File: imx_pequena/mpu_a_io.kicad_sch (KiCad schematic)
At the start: 1 part, among them U1 MCIMX6Z0DVM09AB

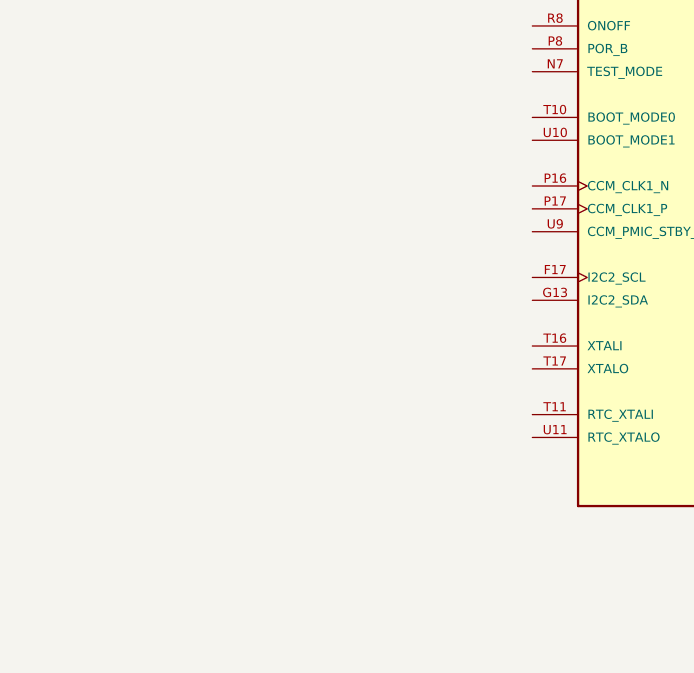
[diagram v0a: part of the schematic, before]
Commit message: Started IO section
began adding crystals
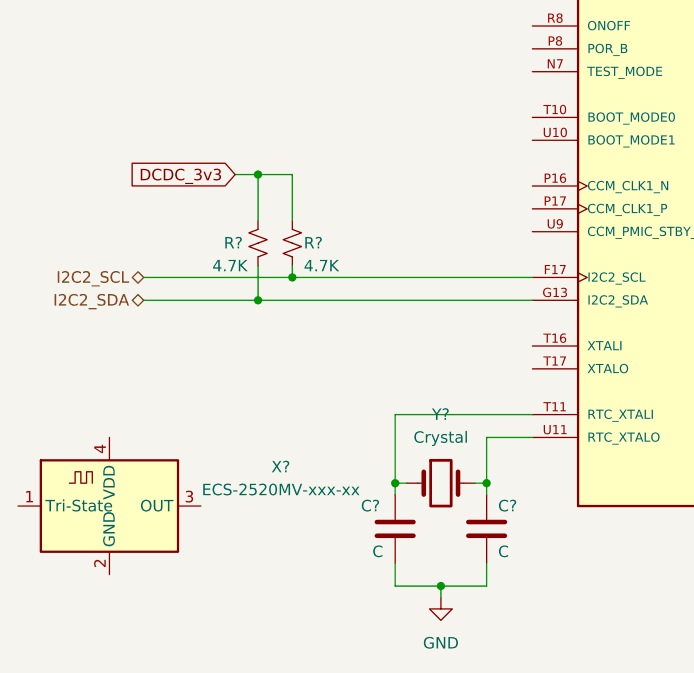
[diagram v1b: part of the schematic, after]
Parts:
- added C? (x2): C, symbol Device:C
- added R? (x2): 4.7K, symbol Device:R_Small_US
- added X?: ECS-2520MV-xxx-xx, Oscillator:Oscillator_SMD_ECS_2520MV-xxx-xx-4Pin_2.5x2.0mm, symbol Oscillator:ECS-2520MV-xxx-xx
- added Y?: Crystal, symbol Device:Crystal
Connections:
- net I2C2_SCL: now reaches U1.F17 (I2C2_SCL)
- net I2C2_SCL: now also R?.2
- net I2C2_SDA: now reaches U1.G13 (I2C2_SDA)
- net I2C2_SDA: now also R?.2
- net at U1.T11 (RTC_XTALI): now also C?.1, Y?.1
- net at U1.U11 (RTC_XTALO): now also C?.1, Y?.2
- new net DCDC_3v3: R?.1, R?.1
- new net GND: C?.2, C?.2
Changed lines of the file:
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@@
 (kicad_sch (version 20211123) (generator eeschema)
   (paper "A4")
+  (junction (at 93.98 114.3) (diameter 0) (color 0 0 0 0)
+  )
+  (junction (at 104.14 114.3) (diameter 0) (color 0 0 0 0)
+  )
+  (junction (at 82.55 91.44) (diameter 0) (color 0 0 0 0)
+  )
+  (junction (at 78.74 93.98) (diameter 0) (color 0 0 0 0)
+  )
+  (junction (at 78.74 80.01) (diameter 0) (color 0 0 0 0)
+  )
+  (junction (at 99.06 125.73) (diameter 0) (color 0 0 0 0)
+  )
+  (wire (pts (xy 93.98 114.3) (xy 93.98 115.57))
+    (stroke (width 0) (type default) (color 0 0 0 0))
+  )
+  (wire (pts (xy 109.22 93.98) (xy 78.74 93.98))
+    (stroke (width 0) (type default) (color 0 0 0 0))
+  )
+  (wire (pts (xy 102.87 114.3) (xy 104.14 114.3))
+    (stroke (width 0) (type default) (color 0 0 0 0))
+  )
+  (wire (pts (xy 93.98 106.68) (xy 93.98 114.3))
+    (stroke (width 0) (type default) (color 0 0 0 0))
+  )
+  (wire (pts (xy 109.22 106.68) (xy 93.98 106.68))
+    (stroke (width 0) (type default) (color 0 0 0 0))
+  )
+  (wire (pts (xy 104.14 109.22) (xy 109.22 109.22))
+    (stroke (width 0) (type default) (color 0 0 0 0))
+  )
+  (wire (pts (xy 104.14 125.73) (xy 104.14 123.19))
+    (stroke (width 0) (type default) (color 0 0 0 0))
+  )
+  (wire (pts (xy 104.14 114.3) (xy 104.14 115.57))
+    (stroke (width 0) (type default) (color 0 0 0 0))
+  )
+  (wire (pts (xy 104.14 114.3) (xy 104.14 109.22))
+    (stroke (width 0) (type default) (color 0 0 0 0))
+  )
+  (wire (pts (xy 78.74 93.98) (xy 78.74 90.17))
+    (stroke (width 0) (type default) (color 0 0 0 0))
+  )
+  (wire (pts (xy 82.55 80.01) (xy 78.74 80.01))
+    (stroke (width 0) (type default) (color 0 0 0 0))
+  )
+  (wire (pts (xy 66.04 93.98) (xy 78.74 93.98))
+    (stroke (width 0) (type default) (color 0 0 0 0))
+  )
+  (wire (pts (xy 99.06 127) (xy 99.06 125.73))
+    (stroke (width 0) (type default) (color 0 0 0 0))
+  )
+  (wire (pts (xy 78.74 80.01) (xy 76.2 80.01))
+    (stroke (width 0) (type default) (color 0 0 0 0))
+  )
+  (wire (pts (xy 109.22 91.44) (xy 82.55 91.44))
+    (stroke (width 0) (type default) (color 0 0 0 0))
+  )
+  (wire (pts (xy 95.25 114.3) (xy 93.98 114.3))
+    (stroke (width 0) (type default) (color 0 0 0 0))
+  )
+  (wire (pts (xy 93.98 125.73) (xy 93.98 123.19))
+    (stroke (width 0) (type default) (color 0 0 0 0))
+  )
+  (wire (pts (xy 99.06 125.73) (xy 104.14 125.73))
+    (stroke (width 0) (type default) (color 0 0 0 0))
+  )
+  (wire (pts (xy 99.06 125.73) (xy 93.98 125.73))
+    (stroke (width 0) (type default) (color 0 0 0 0))
+  )
+  (wire (pts (xy 66.04 91.44) (xy 82.55 91.44))
+    (stroke (width 0) (type default) (color 0 0 0 0))
+  )
+  (wire (pts (xy 82.55 91.44) (xy 82.55 90.17))
+    (stroke (width 0) (type default) (color 0 0 0 0))
+  )
+  (wire (pts (xy 78.74 85.09) (xy 78.74 80.01))
+    (stroke (width 0) (type default) (color 0 0 0 0))
+  )
+  (wire (pts (xy 82.55 85.09) (xy 82.55 80.01))
+    (stroke (width 0) (type default) (color 0 0 0 0))
+  )
+  (global_label "DCDC_3v3" (shape input) (at 76.2 80.01 180) (fields_autoplaced)
+    (effects (font (size 1.27 1.27)) (justify right))
+    (property "Intersheet References" "${INTERSHEET_REFS}" (id 0) (at 64.3526 79.9306 0)
+      (effects (font (size 1.27 1.27)) (justify right) hide)
+    )
+  )
+  (hierarchical_label "I2C2_SDA" (shape bidirectional) (at 66.04 93.98 180)
+    (effects (font (size 1.27 1.27)) (justify right))
+  )
+  (hierarchical_label "I2C2_SCL" (shape bidirectional) (at 66.04 91.44 180)
+    (effects (font (size 1.27 1.27)) (justify right))
+  )
+  (symbol (lib_id "power:GND") (at 99.06 127 0) (unit 1)
+    (in_bom yes) (on_board yes) (fields_autoplaced)
+    (property "Reference" "#PWR?" (id 0) (at 99.06 133.35 0)
+      (effects (font (size 1.27 1.27)) hide)
+    )
+    (property "Value" "GND" (id 1) (at 99.06 132.08 0))
+    (property "Footprint" "" (id 2) (at 99.06 127 0)
+      (effects (font (size 1.27 1.27)) hide)
+    )
+    (property "Datasheet" "" (id 3) (at 99.06 127 0)
+      (effects (font (size 1.27 1.27)) hide)
+    )
+    (pin "1")
+  )
+  (symbol (lib_id "Device:Crystal") (at 99.06 114.3 0) (unit 1)
+    (in_bom yes) (on_board yes) (fields_autoplaced)
+    (property "Reference" "Y?" (id 0) (at 99.06 106.68 0))
+    (property "Value" "Crystal" (id 1) (at 99.06 109.22 0))
+    (property "Footprint" "" (id 2) (at 99.06 114.3 0)
+      (effects (font (size 1.27 1.27)) hide)
+    )
+    (property "Datasheet" "~" (id 3) (at 99.06 114.3 0)
+      (effects (font (size 1.27 1.27)) hide)
+    )
+    (pin "1")
+    (pin "2")
+  )
+  (symbol (lib_id "Device:R_Small_US") (at 78.74 87.63 0) (mirror y) (unit 1)
+    (in_bom yes) (on_board yes)
+    (property "Reference" "R?" (id 0) (at 74.93 87.63 0)
+      (effects (font (size 1.27 1.27)) (justify right))
+    )
+    (property "Value" "4.7K" (id 1) (at 73.66 90.17 0)
+      (effects (font (size 1.27 1.27)) (justify right))
+    )
+    (property "Footprint" "" (id 2) (at 78.74 87.63 0)
+      (effects (font (size 1.27 1.27)) hide)
+    )
+    (property "Datasheet" "~" (id 3) (at 78.74 87.63 0)
+      (effects (font (size 1.27 1.27)) hide)
+    )
+    (pin "1")
+    (pin "2")
+  )
+  (symbol (lib_id "Oscillator:ECS-2520MV-xxx-xx") (at 62.23 116.84 0) (unit 1)
+    (in_bom yes) (on_board yes) (fields_autoplaced)
+    (property "Reference" "X?" (id 0) (at 81.28 112.5093 0))
+    (property "Value" "ECS-2520MV-xxx-xx" (id 1) (at 81.28 115.0493 0))
+    (property "Footprint" "Oscillator:Oscillator_SMD_ECS_2520MV-xxx-xx-4Pin_2.5x2.0mm" (id 2) (at 73.66 125.73 0)
+      (effects (font (size 1.27 1.27)) hide)
+    )
+    (property "Datasheet" "https://www.ecsxtal.com/store/pdf/ECS-2520MV.pdf" (id 3) (at 57.785 113.665 0)
+      (effects (font (size 1.27 1.27)) hide)
+    )
+    (pin "1")
+    (pin "2")
+    (pin "3")
+    (pin "4")
+  )
+  (symbol (lib_id "Device:C") (at 104.14 119.38 0) (unit 1)
+    (in_bom yes) (on_board yes)
+    (property "Reference" "C?" (id 0) (at 105.41 116.84 0)
+      (effects (font (size 1.27 1.27)) (justify left))
+    )
+    (property "Value" "C" (id 1) (at 105.41 121.92 0)
+      (effects (font (size 1.27 1.27)) (justify left))
+    )
+    (property "Footprint" "" (id 2) (at 105.1052 123.19 0)
+      (effects (font (size 1.27 1.27)) hide)
+    )
+    (property "Datasheet" "~" (id 3) (at 104.14 119.38 0)
+      (effects (font (size 1.27 1.27)) hide)
+    )
+    (pin "1")
+    (pin "2")
+  )
+  (symbol (lib_id "Device:C") (at 93.98 119.38 0) (unit 1)
+    (in_bom yes) (on_board yes)
+    (property "Reference" "C?" (id 0) (at 90.17 116.84 0)
+      (effects (font (size 1.27 1.27)) (justify left))
+    )
+    (property "Value" "C" (id 1) (at 91.44 121.92 0)
+      (effects (font (size 1.27 1.27)) (justify left))
+    )
+    (property "Footprint" "" (id 2) (at 94.9452 123.19 0)
+      (effects (font (size 1.27 1.27)) hide)
+    )
+    (property "Datasheet" "~" (id 3) (at 93.98 119.38 0)
+      (effects (font (size 1.27 1.27)) hide)
+    )
+    (pin "1")
+    (pin "2")
+  )
   (symbol (lib_id "MCIMX6Z0DVM09AB:MCIMX6Z0DVM09AB") (at 147.32 86.36 0) (unit 1)
     (in_bom yes) (on_board yes) (fields_autoplaced)
@@
     (pin "U9")
   )
+  (symbol (lib_id "Device:R_Small_US") (at 82.55 87.63 0) (unit 1)
+    (in_bom yes) (on_board yes)
+    (property "Reference" "R?" (id 0) (at 83.82 87.63 0)
+      (effects (font (size 1.27 1.27)) (justify left))
+    )
+    (property "Value" "4.7K" (id 1) (at 83.82 90.17 0)
+      (effects (font (size 1.27 1.27)) (justify left))
+    )
+    (property "Footprint" "" (id 2) (at 82.55 87.63 0)
+      (effects (font (size 1.27 1.27)) hide)
+    )
+    (property "Datasheet" "~" (id 3) (at 82.55 87.63 0)
+      (effects (font (size 1.27 1.27)) hide)
+    )
+    (pin "1")
+    (pin "2")
+  )
 )

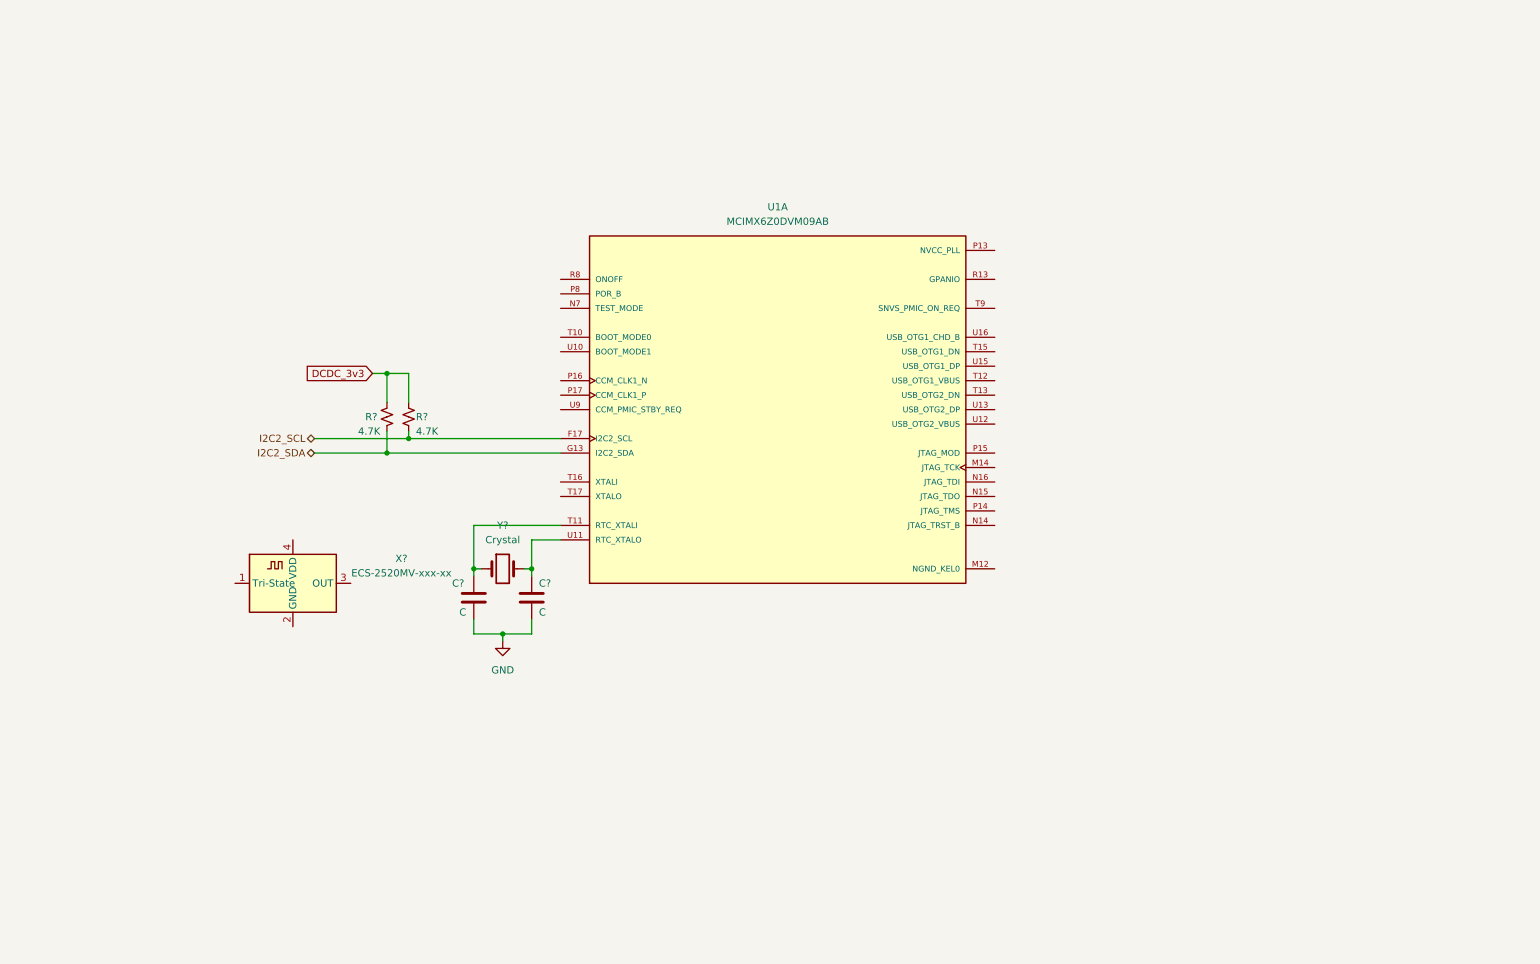
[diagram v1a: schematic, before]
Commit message: misc changes
usb nets, crystal caps, etc...
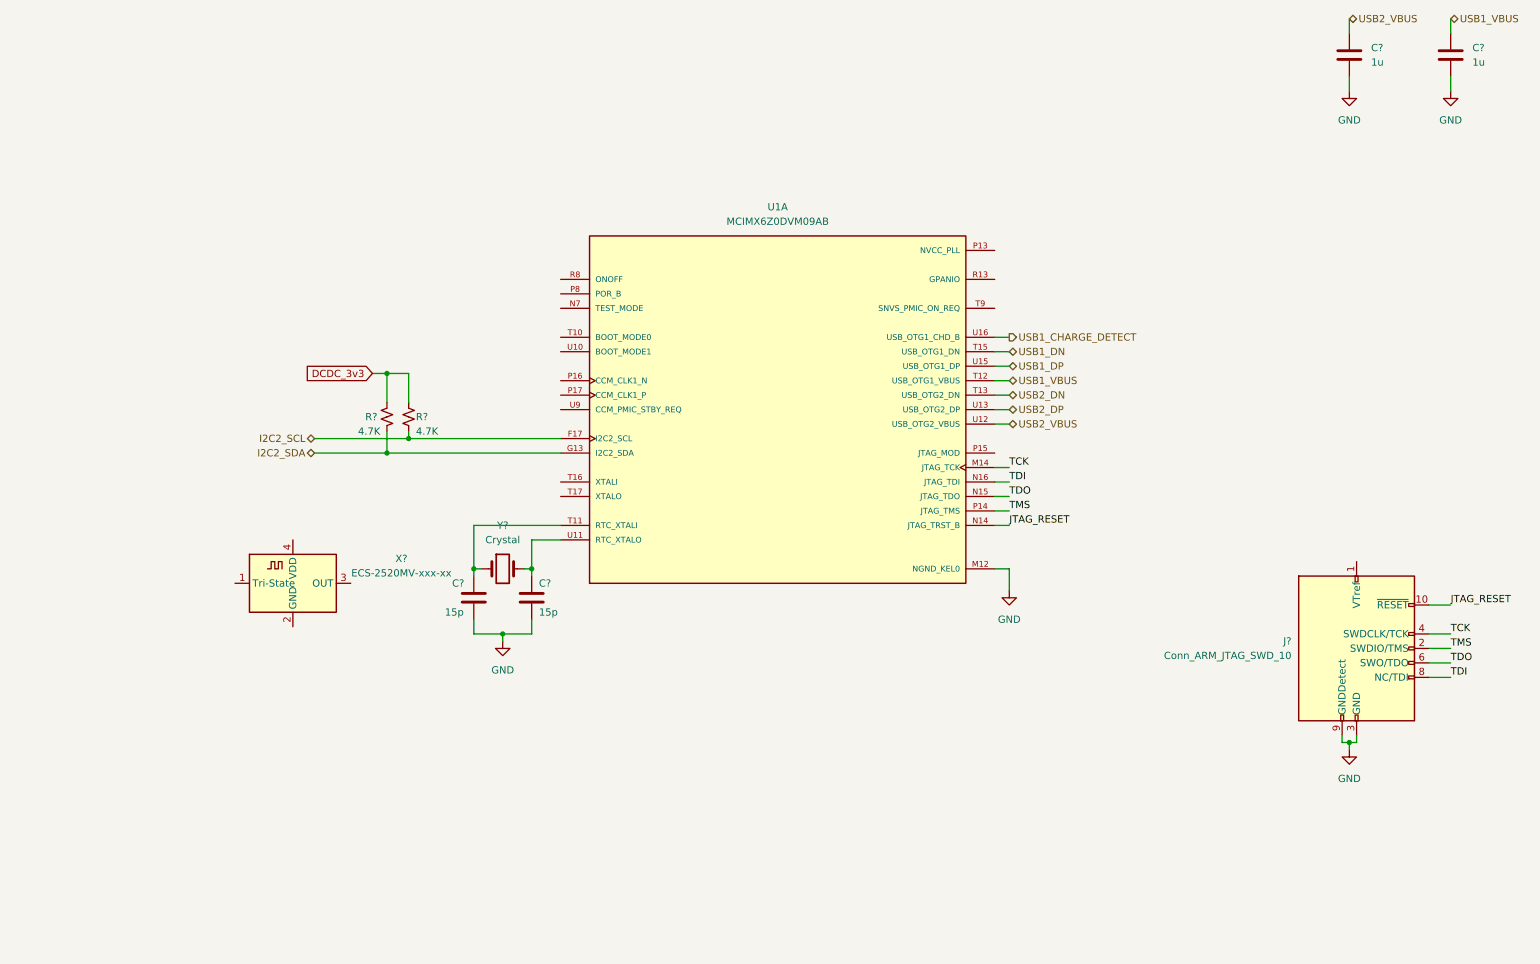
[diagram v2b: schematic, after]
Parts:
- added C? (x2): 1u, symbol Device:C
- added J?: Conn_ARM_JTAG_SWD_10, symbol Connector:Conn_ARM_JTAG_SWD_10
- C? (x2): value C -> 15p
- Y?: PN (none) -> ECS-.327-12.5-16-TR
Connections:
- net GND: now also U1.M12 (NGND_KEL0), C?.2, C?.2, J?.3 (GND), J?.5 (GND), J?.9 (GNDDetect)
- net TCK: now reaches U1.M14 (JTAG_TCK)
- net TCK: now also J?.4 (SWDCLK/TCK)
- net JTAG_RESET: now reaches U1.N14 (JTAG_TRST_B)
- net JTAG_RESET: now also J?.10 (~{RESET})
- net TDO: now reaches U1.N15 (JTAG_TDO)
- net TDO: now also J?.6 (SWO/TDO)
- net TDI: now reaches U1.N16 (JTAG_TDI)
- net TDI: now also J?.8 (NC/TDI)
- net TMS: now reaches U1.P14 (JTAG_TMS)
- net TMS: now also J?.2 (SWDIO/TMS)
- net USB1_VBUS: now reaches U1.T12 (USB_OTG1_VBUS)
- net USB1_VBUS: now also C?.1
- net USB2_DN: now reaches U1.T13 (USB_OTG2_DN)
- net USB1_DN: now reaches U1.T15 (USB_OTG1_DN)
- net USB2_VBUS: now reaches U1.U12 (USB_OTG2_VBUS)
- net USB2_VBUS: now also C?.1
- net USB2_DP: now reaches U1.U13 (USB_OTG2_DP)
- net USB1_DP: now reaches U1.U15 (USB_OTG1_DP)
- net USB1_CHARGE_DETECT: now reaches U1.U16 (USB_OTG1_CHD_B)

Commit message: Power Update
Added 3v3 and 1.35V switchers
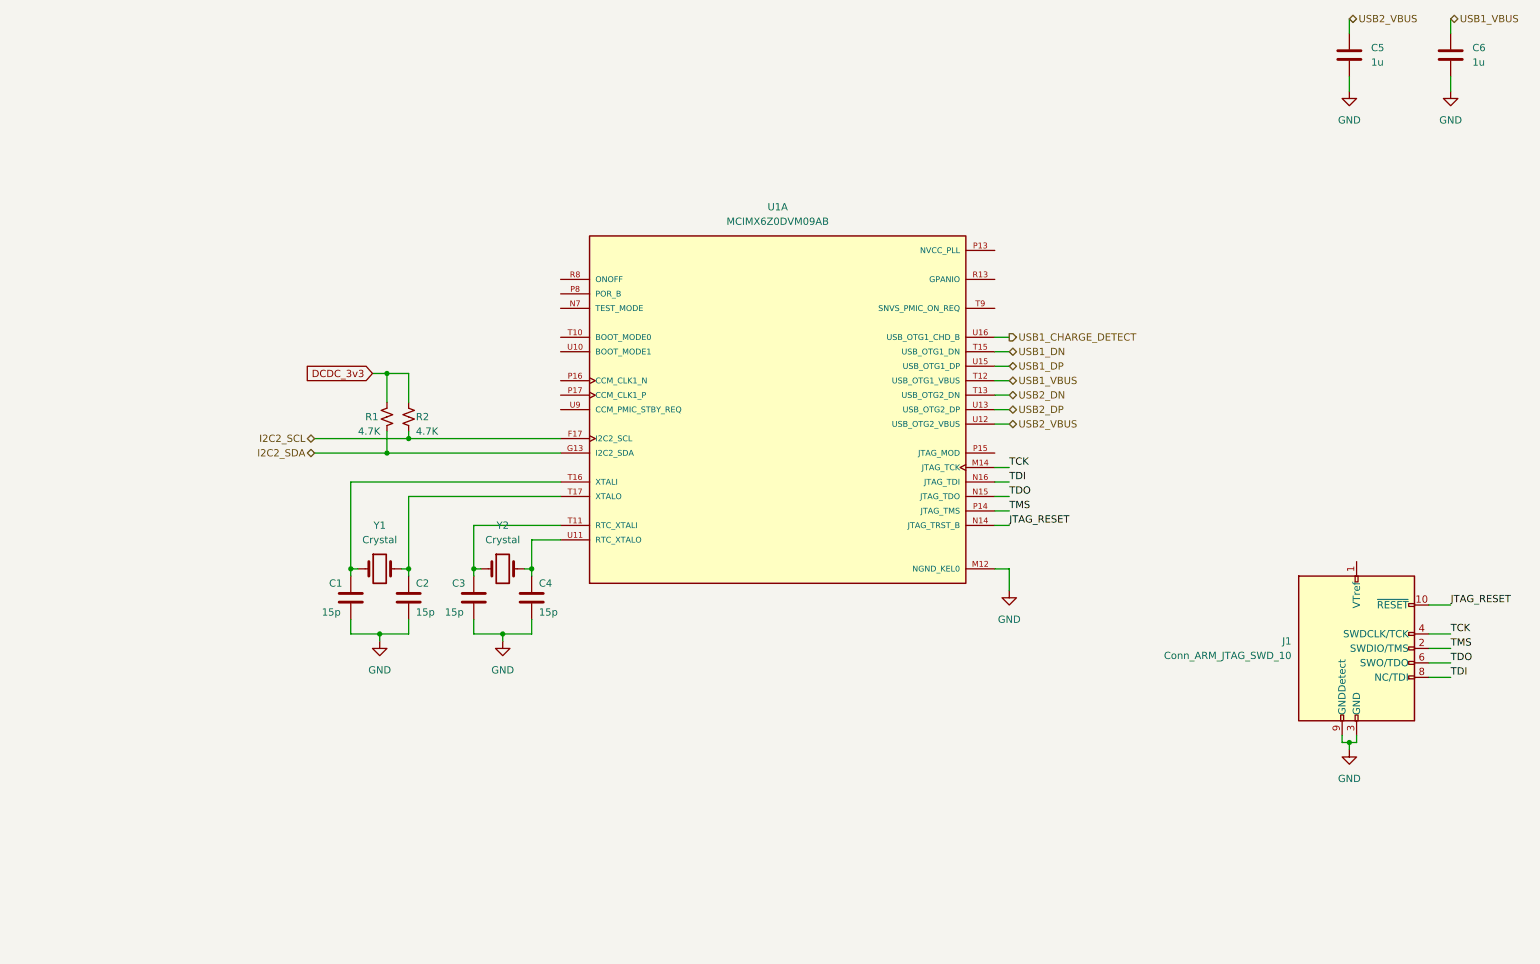
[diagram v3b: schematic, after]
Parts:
- removed X?: ECS-2520MV-xxx-xx, Oscillator:Oscillator_SMD_ECS_2520MV-xxx-xx-4Pin_2.5x2.0mm, symbol Oscillator:ECS-2520MV-xxx-xx
- added C1, C2: 15p, symbol Device:C
- added Y1: Crystal, symbol Device:Crystal
- gave numbers to parts that had none: 8
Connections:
- net GND: now also C1.2, C2.2
- net at U1.T16 (XTALI): now also C1.1, Y1.1
- net at U1.T17 (XTALO): now also C2.1, Y1.2
